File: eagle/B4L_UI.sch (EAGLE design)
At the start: 37 parts

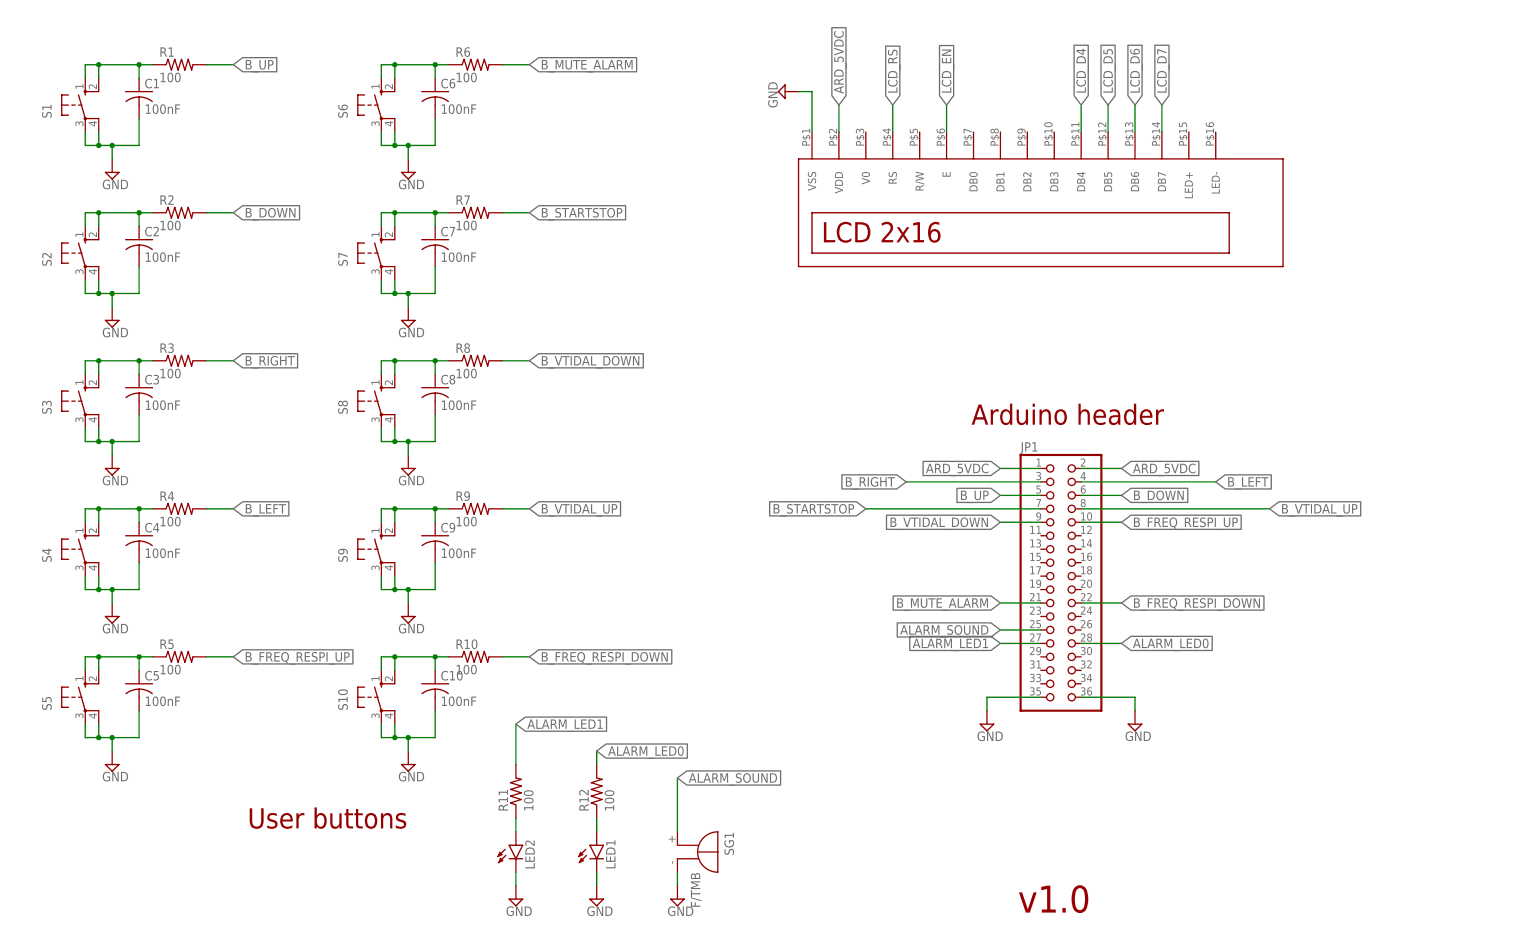
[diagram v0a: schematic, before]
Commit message: Update UI, correct pin mapping
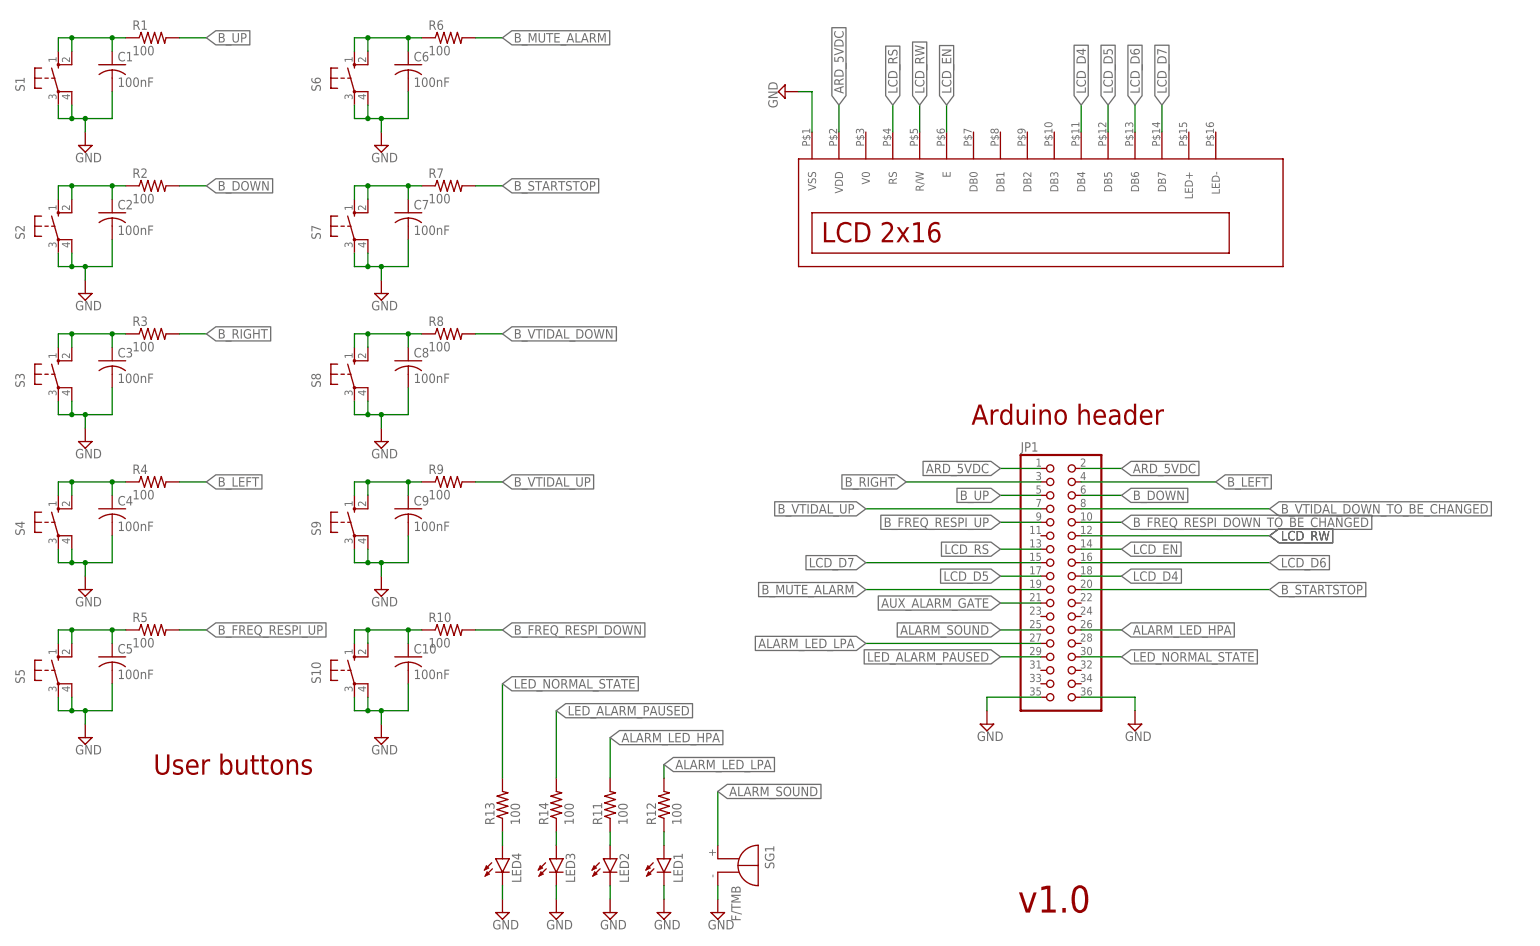
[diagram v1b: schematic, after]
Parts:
- added LED3, LED4: (no value), led:LED5MM
- added R13, R14: 100, rcl:R-US_0309/12
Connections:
- removed net ALARM_LED0: JP1.28, R12.2
- removed net ALARM_LED1: JP1.27, R11.2
- new net ALARM_LED_HPA: JP1.26, R11.2
- new net ALARM_LED_LPA: JP1.27, R12.2
- new net AUX_ALARM_GATE: JP1.21
- new net B_FREQ_RESPI_DOWN_TO_BE_CHANGED: JP1.10
- new net B_VTIDAL_DOWN_TO_BE_CHANGED: JP1.8
- new net LCD_RW: JP1.12, U$1.R/W
- new net LED_ALARM_PAUSED: JP1.29, R14.2
- new net LED_NORMAL_STATE: JP1.30, R13.2
- new net N$6: LED4.A, R13.1
- new net N$8: LED3.A, R14.1
- net B_FREQ_RESPI_DOWN: no longer JP1.22
- net B_FREQ_RESPI_UP: now also JP1.9; no longer JP1.10
- net B_MUTE_ALARM: now also JP1.19; no longer JP1.21
- net B_STARTSTOP: now also JP1.20; no longer JP1.7
- net B_VTIDAL_DOWN: no longer JP1.9
- net B_VTIDAL_UP: now also JP1.7; no longer JP1.8
- net GND: now also LED3.C, LED4.C
- net LCD_D4: now also JP1.18
- net LCD_D5: now also JP1.17
- net LCD_D6: now also JP1.16
- net LCD_D7: now also JP1.15
- net LCD_EN: now also JP1.14
- net LCD_RS: now also JP1.13
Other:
- moved on the sheet: C1, C10, C2, C3, C4, C5, C6, C7, C8, C9, LED1, LED2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

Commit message: Update of LCD connectivity and capacitor values (near buttons)
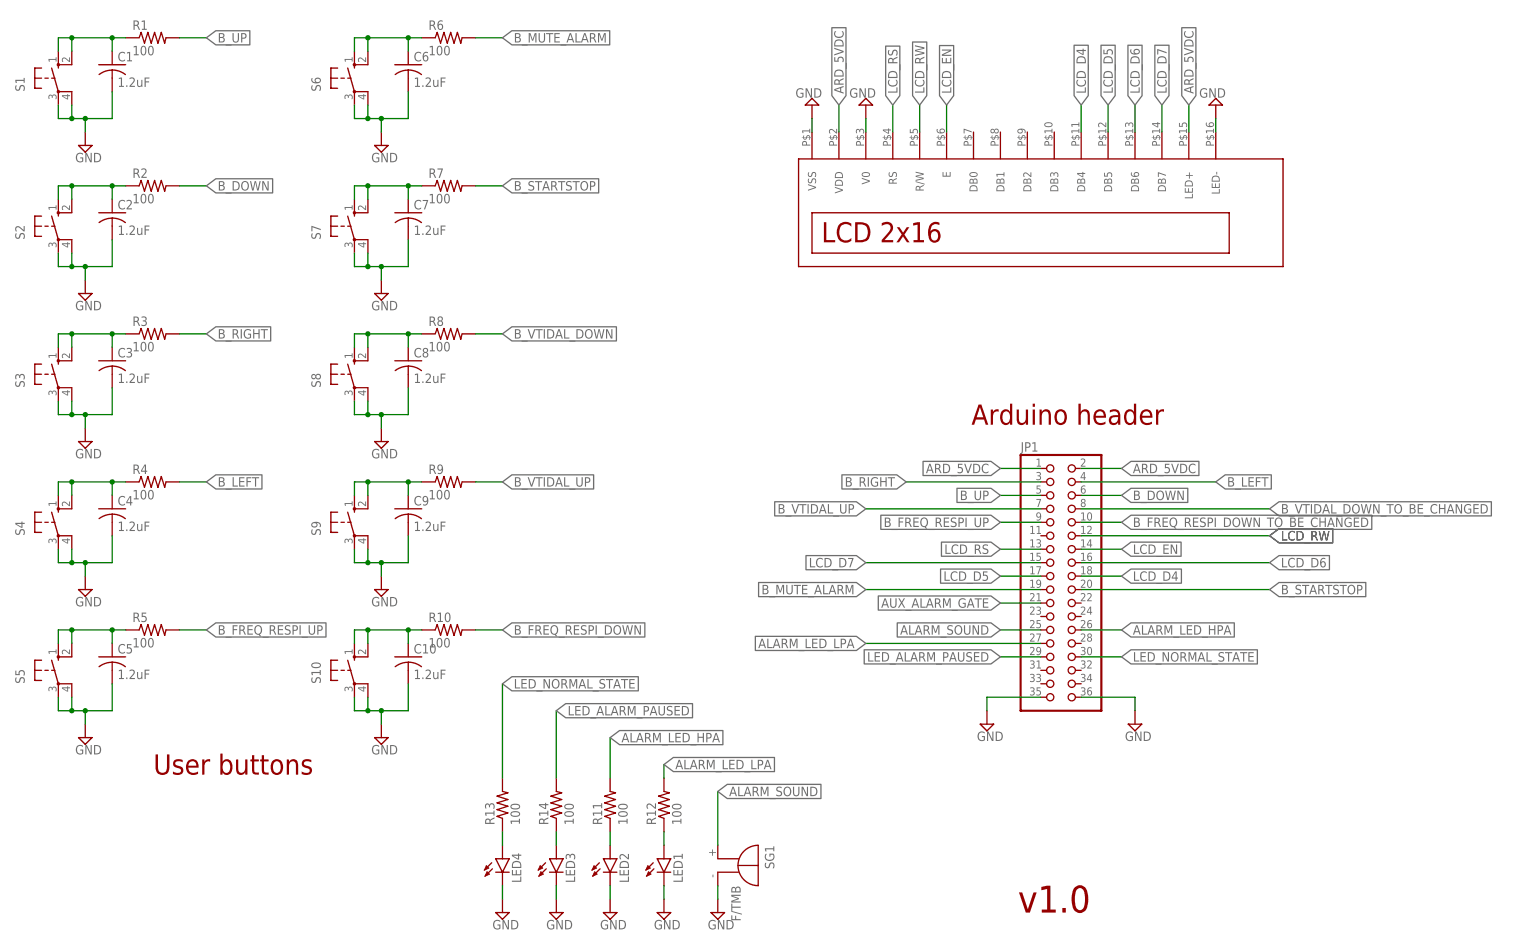
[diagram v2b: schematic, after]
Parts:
- C1, C10, C2, C3, C4, C5, C6, C7, C8, C9: value 100nF -> 1.2uF
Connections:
- net ARD_5VDC: now also U$1.LED+
- net GND: now also U$1.LED-, U$1.V0

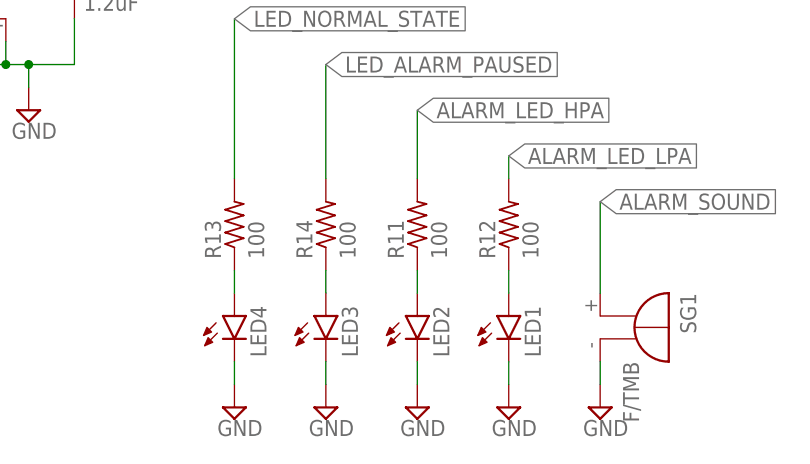
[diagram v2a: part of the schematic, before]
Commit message: [UI board] Update of LEDs and resistors
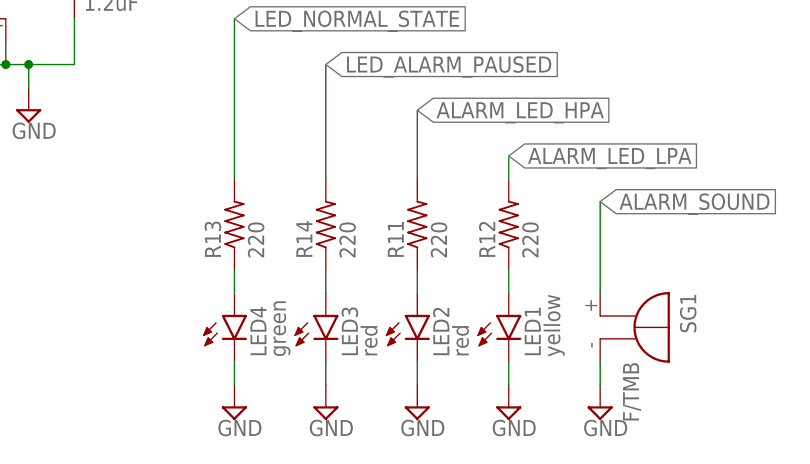
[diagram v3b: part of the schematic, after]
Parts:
- LED1: value (none) -> yellow
- LED2, LED3: value (none) -> red
- LED4: value (none) -> green
- R11, R12, R13, R14: value 100 -> 220
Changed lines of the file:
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@@
 <part name="SUPPLY13" library="supply2" library_urn="urn:adsk.eagle:library:372" deviceset="GND" device=""/>
 <part name="SG1" library="buzzer" library_urn="urn:adsk.eagle:library:113" deviceset="F/TMB" device="" package3d_urn="urn:adsk.eagle:package:5260/1"/>
-<part name="LED1" library="led" library_urn="urn:adsk.eagle:library:259" deviceset="LED" device="5MM" package3d_urn="urn:adsk.eagle:package:15799/2"/>
-<part name="LED2" library="led" library_urn="urn:adsk.eagle:library:259" deviceset="LED" device="5MM" package3d_urn="urn:adsk.eagle:package:15799/2"/>
-<part name="R11" library="rcl" library_urn="urn:adsk.eagle:library:334" deviceset="R-US_" device="0309/12" package3d_urn="urn:adsk.eagle:package:23571/1" value="100"/>
-<part name="R12" library="rcl" library_urn="urn:adsk.eagle:library:334" deviceset="R-US_" device="0309/12" package3d_urn="urn:adsk.eagle:package:23571/1" value="100"/>
+<part name="LED1" library="led" library_urn="urn:adsk.eagle:library:259" deviceset="LED" device="5MM" package3d_urn="urn:adsk.eagle:package:15799/2" value="yellow"/>
+<part name="LED2" library="led" library_urn="urn:adsk.eagle:library:259" deviceset="LED" device="5MM" package3d_urn="urn:adsk.eagle:package:15799/2" value="red"/>
+<part name="R11" library="rcl" library_urn="urn:adsk.eagle:library:334" deviceset="R-US_" device="0309/12" package3d_urn="urn:adsk.eagle:package:23571/1" value="220"/>
+<part name="R12" library="rcl" library_urn="urn:adsk.eagle:library:334" deviceset="R-US_" device="0309/12" package3d_urn="urn:adsk.eagle:package:23571/1" value="220"/>
 <part name="SUPPLY14" library="supply2" library_urn="urn:adsk.eagle:library:372" deviceset="GND" device=""/>
 <part name="SUPPLY15" library="supply2" library_urn="urn:adsk.eagle:library:372" deviceset="GND" device=""/>
 <part name="SUPPLY16" library="supply2" library_urn="urn:adsk.eagle:library:372" deviceset="GND" device=""/>
-<part name="LED3" library="led" library_urn="urn:adsk.eagle:library:259" deviceset="LED" device="5MM" package3d_urn="urn:adsk.eagle:package:15799/2"/>
-<part name="LED4" library="led" library_urn="urn:adsk.eagle:library:259" deviceset="LED" device="5MM" package3d_urn="urn:adsk.eagle:package:15799/2"/>
-<part name="R13" library="rcl" library_urn="urn:adsk.eagle:library:334" deviceset="R-US_" device="0309/12" package3d_urn="urn:adsk.eagle:package:23571/1" value="100"/>
-<part name="R14" library="rcl" library_urn="urn:adsk.eagle:library:334" deviceset="R-US_" device="0309/12" package3d_urn="urn:adsk.eagle:package:23571/1" value="100"/>
+<part name="LED3" library="led" library_urn="urn:adsk.eagle:library:259" deviceset="LED" device="5MM" package3d_urn="urn:adsk.eagle:package:15799/2" value="red"/>
+<part name="LED4" library="led" library_urn="urn:adsk.eagle:library:259" deviceset="LED" device="5MM" package3d_urn="urn:adsk.eagle:package:15799/2" value="green"/>
+<part name="R13" library="rcl" library_urn="urn:adsk.eagle:library:334" deviceset="R-US_" device="0309/12" package3d_urn="urn:adsk.eagle:package:23571/1" value="220"/>
+<part name="R14" library="rcl" library_urn="urn:adsk.eagle:library:334" deviceset="R-US_" device="0309/12" package3d_urn="urn:adsk.eagle:package:23571/1" value="220"/>
 <part name="SUPPLY17" library="supply2" library_urn="urn:adsk.eagle:library:372" deviceset="GND" device=""/>
 <part name="SUPPLY18" library="supply2" library_urn="urn:adsk.eagle:library:372" deviceset="GND" device=""/>

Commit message: [UI board] Addition of ACK button
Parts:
- removed R12, R13, R14: 220, rcl:R-US_0309/12
- added C11: 1.2uF, rcl:C-US050-050X075
- added RLED1, RLED2, RLED3, RLED4: 220, rcl:R-US_0309/12
- added S11: (no value), switch-omron:40-XX
- LED1: value yellow -> green
- LED4: value green -> yellow
- R11: value 220 -> 100
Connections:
- new net B_ACK_ALARM: R11.2
- new net N$10: C11.1, R11.1, S11.S, S11.S1
- net ALARM_LED_HPA: now also RLED3.2; no longer R11.2
- net ALARM_LED_LPA: now also RLED4.2; no longer R12.2
- net B_FREQ_RESPI_DOWN: now also R6.2; no longer R10.2
- net B_MUTE_ALARM: now also R9.2; no longer R6.2
- net B_STARTSTOP: now also R10.2; no longer R7.2
- net B_VTIDAL_UP: now also R7.2; no longer R9.2
- net GND: now also C11.2, S11.P, S11.P1
- net LED_ALARM_PAUSED: now also RLED2.2; no longer R14.2
- net LED_NORMAL_STATE: now also RLED1.2; no longer R13.2
- net N$2: now also LED3.A, RLED3.1; no longer LED2.A, R11.1
- net N$4: now also LED4.A, RLED4.1; no longer LED1.A, R12.1
- net N$6: now also LED1.A, RLED1.1; no longer LED4.A, R13.1
- net N$8: now also LED2.A, RLED2.1; no longer LED3.A, R14.1
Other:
- note added: "Alarm part"
- note added: "LCD screen"
- note added: "LEDs"

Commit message: [UI board] Update of Arduino pin header connectivity
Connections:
- removed net ALARM_LED_HPA: JP1.26, RLED3.2
- removed net ALARM_LED_LPA: JP1.27, RLED4.2
- removed net AUX_ALARM_GATE: JP1.21
- removed net B_ACK_ALARM: R11.2
- removed net B_FREQ_RESPI_DOWN_TO_BE_CHANGED: JP1.10
- removed net B_MUTE_ALARM: JP1.19, R9.2
- removed net B_VTIDAL_DOWN_TO_BE_CHANGED: JP1.8
- new net B_ALARM_ACK: JP1.15, R11.2
- new net B_ALARM_MUTE: JP1.18, R9.2
- new net LED_ALARM_HPA: JP1.11, RLED3.2
- new net LED_ALARM_LPA: JP1.10, RLED4.2
- net ALARM_SOUND: no longer JP1.25
- net ARD_5VDC: now also JP1.35, JP1.36; no longer JP1.1, JP1.2
- net B_DOWN: now also JP1.31; no longer JP1.6
- net B_FREQ_RESPI_DOWN: now also JP1.29
- net B_FREQ_RESPI_UP: now also JP1.28; no longer JP1.9
- net B_LEFT: now also JP1.33; no longer JP1.4
- net B_RIGHT: now also JP1.34; no longer JP1.3
- net B_STARTSTOP: now also JP1.17; no longer JP1.20
- net B_UP: now also JP1.32; no longer JP1.5
- net B_VTIDAL_DOWN: now also JP1.27
- net B_VTIDAL_UP: now also JP1.30; no longer JP1.7
- net GND: now also JP1.1, JP1.2; no longer JP1.35, JP1.36
- net LCD_D4: now also JP1.19; no longer JP1.18
- net LCD_D5: now also JP1.20; no longer JP1.17
- net LCD_D6: now also JP1.21; no longer JP1.16
- net LCD_D7: now also JP1.22; no longer JP1.15
- net LCD_EN: now also JP1.23; no longer JP1.14
- net LCD_RS: now also JP1.24; no longer JP1.13
- net LCD_RW: now also JP1.25; no longer JP1.12
- net LED_ALARM_PAUSED: now also JP1.8; no longer JP1.29
- net LED_NORMAL_STATE: now also JP1.7; no longer JP1.30
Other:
- note added: "Alarm part (TO UPDATE)"
- note added: "Arduino header (IO pins 23-53)"
- note removed: "Alarm part"
- note removed: "Arduino header"
- moved on the sheet: SG1
